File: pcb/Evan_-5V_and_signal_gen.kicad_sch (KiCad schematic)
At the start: 24 parts, among them IC1 TL7660IDGKR, IC2 TL081IDT, IC4 UA78M33CDCYG3, J2 M22-6003005

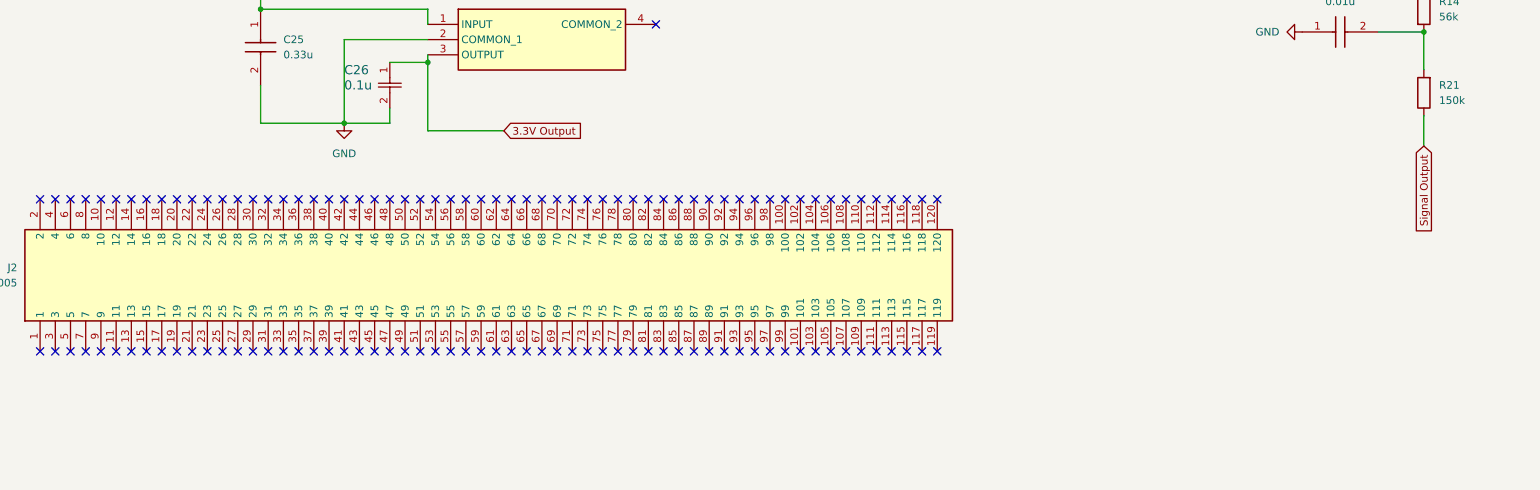
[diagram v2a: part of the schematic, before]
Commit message: First Major PCB layout and routing (#10)
* first bulk commit of routing

* removed about 300 pcb ERC warnings

* removed all pcb DRC errors/warnings

* silkscreen: remove part num from inside part, cleanup

* add silk labels for each pin, my final cleanup

* remove all errors and suppress unspecified connections warnings in schematic ERC

---------

Co-authored-by: evanc2987 <evan.campbell2987@gmail.com>
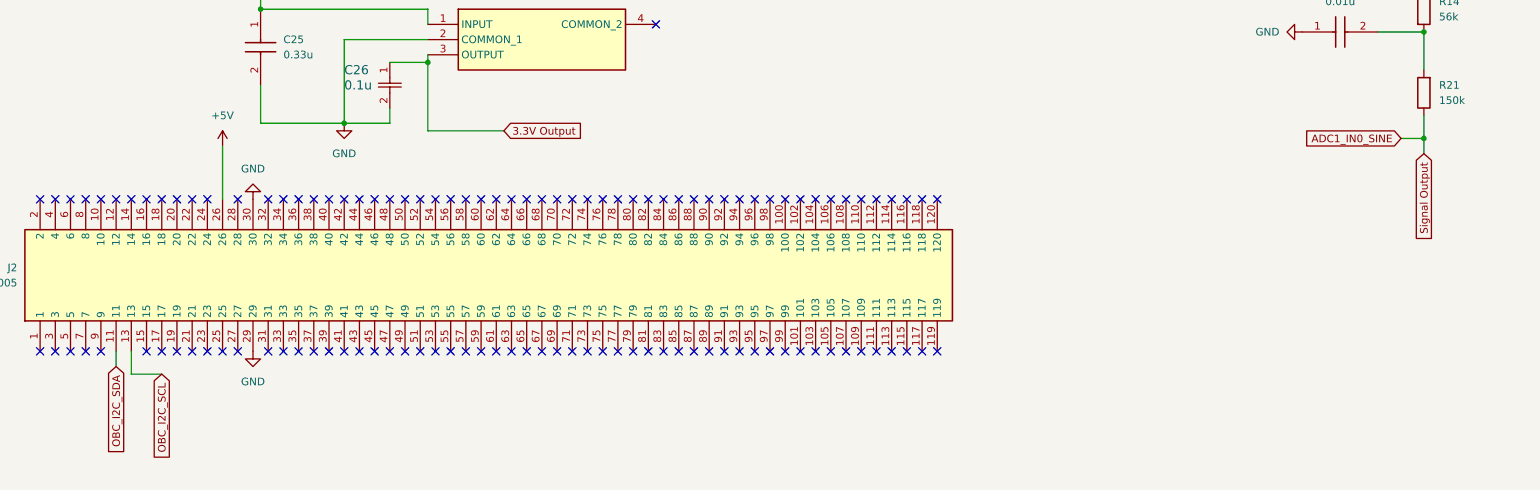
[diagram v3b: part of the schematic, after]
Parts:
- C12, C13: footprint T495D -> (none)
- C17, C18, C25: footprint C0805 -> (none)
- IC1: footprint SOP65P490X110-8N -> capstone:SOIC127P600X175-8N
- IC2: footprint SOIC127P600X175-8N -> capstone:SOIC127P600X175-8N
- IC4: footprint SOT230P700X180-4N -> (none)
- J2: footprint RHDR120W55P200_4X30_6020X800X935P -> capstone:RHDR120W55P200_4X30_6020X800X935P
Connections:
- net +5V: now also J2.26
- net GND: now also J2.29, J2.30
- net OBC_I2C_SDA: now reaches J2.11
- net OBC_I2C_SCL: now reaches J2.13
- net Signal Output renamed ADC1_IN0_SINE
- no-connect marks 124 -> 119
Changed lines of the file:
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@@
   (junction (at 82.55 38.1) (diameter 0) (color 0 0 0 0)
+  )
+  (junction (at 262.89 123.19) (diameter 0) (color 0 0 0 0)
   )
   (junction (at 156.21 22.86) (diameter 0) (color 0 0 0 0)
@@
   (no_connect (at 85.09 133.35))
   (no_connect (at 97.79 133.35))
-  (no_connect (at 69.85 133.35))
   (no_connect (at 92.71 133.35))
   (no_connect (at 39.37 158.75))
@@
   (no_connect (at 146.05 133.35))
   (no_connect (at 46.99 133.35))
-  (no_connect (at 44.45 158.75))
   (no_connect (at 176.53 133.35))
   (no_connect (at 176.53 158.75))
@@
   (no_connect (at 163.83 133.35))
   (no_connect (at 49.53 158.75))
-  (no_connect (at 67.31 133.35))
   (no_connect (at 123.19 133.35))
   (no_connect (at 77.47 133.35))
@@
   (no_connect (at 41.91 158.75))
   (no_connect (at 80.01 158.75))
+  (no_connect (at 69.85 133.35))
   (no_connect (at 166.37 133.35))
   (no_connect (at 171.45 133.35))
   (no_connect (at 74.93 158.75))
   (no_connect (at 64.77 133.35))
+  (no_connect (at 82.55 158.75))
   (no_connect (at 138.43 133.35))
   (no_connect (at 181.61 133.35))
@@
   (no_connect (at 80.01 133.35))
   (no_connect (at 138.43 158.75))
-  (no_connect (at 46.99 158.75))
   (no_connect (at 123.19 158.75))
   (no_connect (at 171.45 158.75))
@@
   (no_connect (at 77.47 158.75))
   (no_connect (at 100.33 158.75))
-  (no_connect (at 67.31 158.75))
   (no_connect (at 69.85 158.75))
   (no_connect (at 148.59 133.35))
@@
   (no_connect (at 52.07 133.35))
   (no_connect (at 59.69 158.75))
-  (no_connect (at 82.55 158.75))
   (no_connect (at 34.29 158.75))
   (no_connect (at 59.69 133.35))
-  (no_connect (at 62.23 133.35))
   (no_connect (at 41.91 133.35))
   (no_connect (at 49.53 133.35))
   (no_connect (at 102.87 158.75))
   (no_connect (at 54.61 133.35))
+  (no_connect (at 85.09 158.75))
   (no_connect (at 115.57 133.35))
   (no_connect (at 110.49 133.35))
@@
   (no_connect (at 95.25 158.75))
   (no_connect (at 97.79 158.75))
-  (no_connect (at 85.09 158.75))
   (no_connect (at 153.67 133.35))
   (no_connect (at 90.17 158.75))
@@
     (stroke (width 0) (type default))
   )
+  (wire (pts (xy 44.45 158.75) (xy 44.45 161.29))
+    (stroke (width 0) (type default))
+  )
   (wire (pts (xy 95.25 35.56) (xy 73.66 35.56))
     (stroke (width 0) (type default))
@@
     (stroke (width 0) (type default))
   )
+  (wire (pts (xy 262.89 123.19) (xy 262.89 125.73))
+    (stroke (width 0) (type default))
+  )
   (wire (pts (xy 104.14 38.1) (xy 113.03 38.1))
     (stroke (width 0) (type default))
@@
     (stroke (width 0) (type default))
   )
+  (wire (pts (xy 46.99 162.56) (xy 46.99 158.75))
+    (stroke (width 0) (type default))
+  )
   (wire (pts (xy 217.17 71.12) (xy 262.89 71.12))
     (stroke (width 0) (type default))
@@
     (stroke (width 0) (type default))
   )
+  (wire (pts (xy 259.08 123.19) (xy 262.89 123.19))
+    (stroke (width 0) (type default))
+  )
   (wire (pts (xy 158.75 71.12) (xy 147.32 71.12))
     (stroke (width 0) (type default))
@@
     (stroke (width 0) (type default))
   )
+  (wire (pts (xy 52.07 162.56) (xy 46.99 162.56))
+    (stroke (width 0) (type default))
+  )
   (wire (pts (xy 82.55 38.1) (xy 104.14 38.1))
     (stroke (width 0) (type default))
@@
     (stroke (width 0) (type default))
   )
-  (wire (pts (xy 262.89 119.38) (xy 262.89 124.46))
-    (stroke (width 0) (type default))
-  )
-  (global_label "Signal Output" (shape input) (at 262.89 124.46 270) (fields_autoplaced)
+  (wire (pts (xy 62.23 124.46) (xy 62.23 133.35))
+    (stroke (width 0) (type default))
+  )
+  (wire (pts (xy 262.89 119.38) (xy 262.89 123.19))
+    (stroke (width 0) (type default))
+  )
+  (global_label "ADC1_IN0_SINE" (shape input) (at 259.08 123.19 180) (fields_autoplaced)
     (effects (font (size 1.27 1.27)) (justify right))
-    (property "Intersheetrefs" "${INTERSHEET_REFS}" (at 262.89 140.5682 90)
+    (property "Intersheetrefs" "${INTERSHEET_REFS}" (at 241.8829 123.19 0)
+      (effects (font (size 1.27 1.27)) (justify right) hide)
+    )
+  )
+  (global_label "Signal Output" (shape input) (at 262.89 125.73 270) (fields_autoplaced)
+    (effects (font (size 1.27 1.27)) (justify right))
+    (property "Intersheetrefs" "${INTERSHEET_REFS}" (at 262.89 141.8382 90)
       (effects (font (size 1.27 1.27)) (justify right) hide)
     )
@@
     )
   )
+  (global_label "OBC_I2C_SDA" (shape input) (at 44.45 161.29 270) (fields_autoplaced)
+    (effects (font (size 1.27 1.27)) (justify right))
+    (property "Intersheetrefs" "${INTERSHEET_REFS}" (at 44.45 176.7333 90)
+      (effects (font (size 1.27 1.27)) (justify right) hide)
+    )
+  )
+  (global_label "OBC_I2C_SCL" (shape input) (at 52.07 162.56 270) (fields_autoplaced)
+    (effects (font (size 1.27 1.27)) (justify right))
+    (property "Intersheetrefs" "${INTERSHEET_REFS}" (at 52.07 177.9428 90)
+      (effects (font (size 1.27 1.27)) (justify right) hide)
+    )
+  )
   (global_label "3.3V Output" (shape input) (at 109.22 121.92 0) (fields_autoplaced)
     (effects (font (size 1.27 1.27)) (justify left))
@@
       (effects (font (size 1.27 1.27)) (justify right))
     )
-    (property "Footprint" "T495D" (at 178.74 44.45 0)
+    (property "Footprint" "" (at 178.74 44.45 0)
       (effects (font (size 1.27 1.27)) (justify left top) hide)
     )
@@
       (effects (font (size 1.27 1.27)) (justify left))
     )
-    (property "Footprint" "RHDR120W55P200_4X30_6020X800X935P" (at 126.67 137.16 0)
+    (property "Footprint" "capstone:RHDR120W55P200_4X30_6020X800X935P" (at 126.67 137.16 0)
       (effects (font (size 1.27 1.27)) (justify left top) hide)
     )
@@
     )
   )
+  (symbol (lib_id "power:GND") (at 67.31 158.75 0) (unit 1)
+    (in_bom yes) (on_board yes) (dnp no) (fields_autoplaced)
+    (property "Reference" "#PWR014" (at 67.31 165.1 0)
+      (effects (font (size 1.27 1.27)) hide)
+    )
+    (property "Value" "GND" (at 67.31 163.83 0)
+      (effects (font (size 1.27 1.27)))
+    )
+    (property "Footprint" "" (at 67.31 158.75 0)
+      (effects (font (size 1.27 1.27)) hide)
+    )
+    (property "Datasheet" "" (at 67.31 158.75 0)
+      (effects (font (size 1.27 1.27)) hide)
+    )
+    (pin "1")
+    (instances
+      (project "mcu_integration"
+        (path "/c0210bc3-f67f-47d8-a34e-f002a728adb2/39708197-8fe0-4b5c-ba49-65ed06982da9"
+          (reference "#PWR014") (unit 1)
+        )
+      )
+    )
+  )
   (symbol (lib_id "capstone:TL7660IDGKR") (at 43.18 30.48 0) (unit 1)
     (in_bom yes) (on_board yes) (dnp no) (fields_autoplaced)
@@
       (effects (font (size 1.27 1.27)))
     )
-    (property "Footprint" "SOP65P490X110-8N" (at 69.85 125.4 0)
+    (property "Footprint" "capstone:SOIC127P600X175-8N" (at 69.85 125.4 0)
       (effects (font (size 1.27 1.27)) (justify left top) hide)
     )
@@
       (effects (font (size 1.27 1.27)))
     )
-    (property "Footprint" "SOIC127P600X175-8N" (at 213.36 160.96 0)
+    (property "Footprint" "capstone:SOIC127P600X175-8N" (at 213.36 160.96 0)
       (effects (font (size 1.27 1.27)) (justify left top) hide)
     )
@@
       (effects (font (size 1.27 1.27)) (justify right))
     )
-    (property "Footprint" "C0805" (at 243.51 26.67 0)
+    (property "Footprint" "" (at 243.51 26.67 0)
       (effects (font (size 1.27 1.27)) (justify left top) hide)
     )
@@
       (effects (font (size 1.27 1.27)) (justify left))
     )
-    (property "Footprint" "T495D" (at -80.95 38.1 0)
+    (property "Footprint" "" (at -80.95 38.1 0)
       (effects (font (size 1.27 1.27)) (justify left top) hide)
     )
@@
       (effects (font (size 1.27 1.27)))
     )
-    (property "Footprint" "C0805" (at 251.46 201.6 0)
+    (property "Footprint" "" (at 251.46 201.6 0)
       (effects (font (size 1.27 1.27)) (justify left top) hide)
     )
@@
       (effects (font (size 1.27 1.27)) (justify left))
     )
-    (property "Footprint" "C0805" (at -27.61 110.49 0)
+    (property "Footprint" "" (at -27.61 110.49 0)
       (effects (font (size 1.27 1.27)) (justify left top) hide)
     )
@@
     )
   )
+  (symbol (lib_id "power:GND") (at 67.31 133.35 180) (unit 1)
+    (in_bom yes) (on_board yes) (dnp no) (fields_autoplaced)
+    (property "Reference" "#PWR02" (at 67.31 127 0)
+      (effects (font (size 1.27 1.27)) hide)
+    )
+    (property "Value" "GND" (at 67.31 128.27 0)
+      (effects (font (size 1.27 1.27)))
+    )
+    (property "Footprint" "" (at 67.31 133.35 0)
+      (effects (font (size 1.27 1.27)) hide)
+    )
+    (property "Datasheet" "" (at 67.31 133.35 0)
+      (effects (font (size 1.27 1.27)) hide)
+    )
+    (pin "1")
+    (instances
+      (project "mcu_integration"
+        (path "/c0210bc3-f67f-47d8-a34e-f002a728adb2/39708197-8fe0-4b5c-ba49-65ed06982da9"
+          (reference "#PWR02") (unit 1)
+        )
+      )
+    )
+  )
   (symbol (lib_id "power:GND") (at 129.54 81.28 0) (unit 1)
     (in_bom yes) (on_board yes) (dnp no) (fields_autoplaced)
@@
       (effects (font (size 1.27 1.27)))
     )
-    (property "Footprint" "SOT230P700X180-4N" (at 130.81 199.06 0)
+    (property "Footprint" "" (at 130.81 199.06 0)
       (effects (font (size 1.27 1.27)) (justify left top) hide)
     )
@@
         )
       )
+    )
+  )
+  (symbol (lib_id "power:+5V") (at 62.23 124.46 0) (unit 1)
+    (in_bom yes) (on_board yes) (dnp no) (fields_autoplaced)
+    (property "Reference" "#PWR016" (at 62.23 128.27 0)
+      (effects (font (size 1.27 1.27)) hide)
+    )
+    (property "Value" "+5V" (at 62.23 119.38 0)
+      (effects (font (size 1.27 1.27)))
+    )
+    (property "Footprint" "" (at 62.23 124.46 0)
+      (effects (font (size 1.27 1.27)) hide)
+    )
+    (property "Datasheet" "" (at 62.23 124.46 0)
+      (effects (font (size 1.27 1.27)) hide)
+    )
+    (pin "1")
+    (instances
+      (project "mcu_integration"
+        (path "/c0210bc3-f67f-47d8-a34e-f002a728adb2/39708197-8fe0-4b5c-ba49-65ed06982da9"
+          (reference "#PWR016") (unit 1)
+        )
+      )

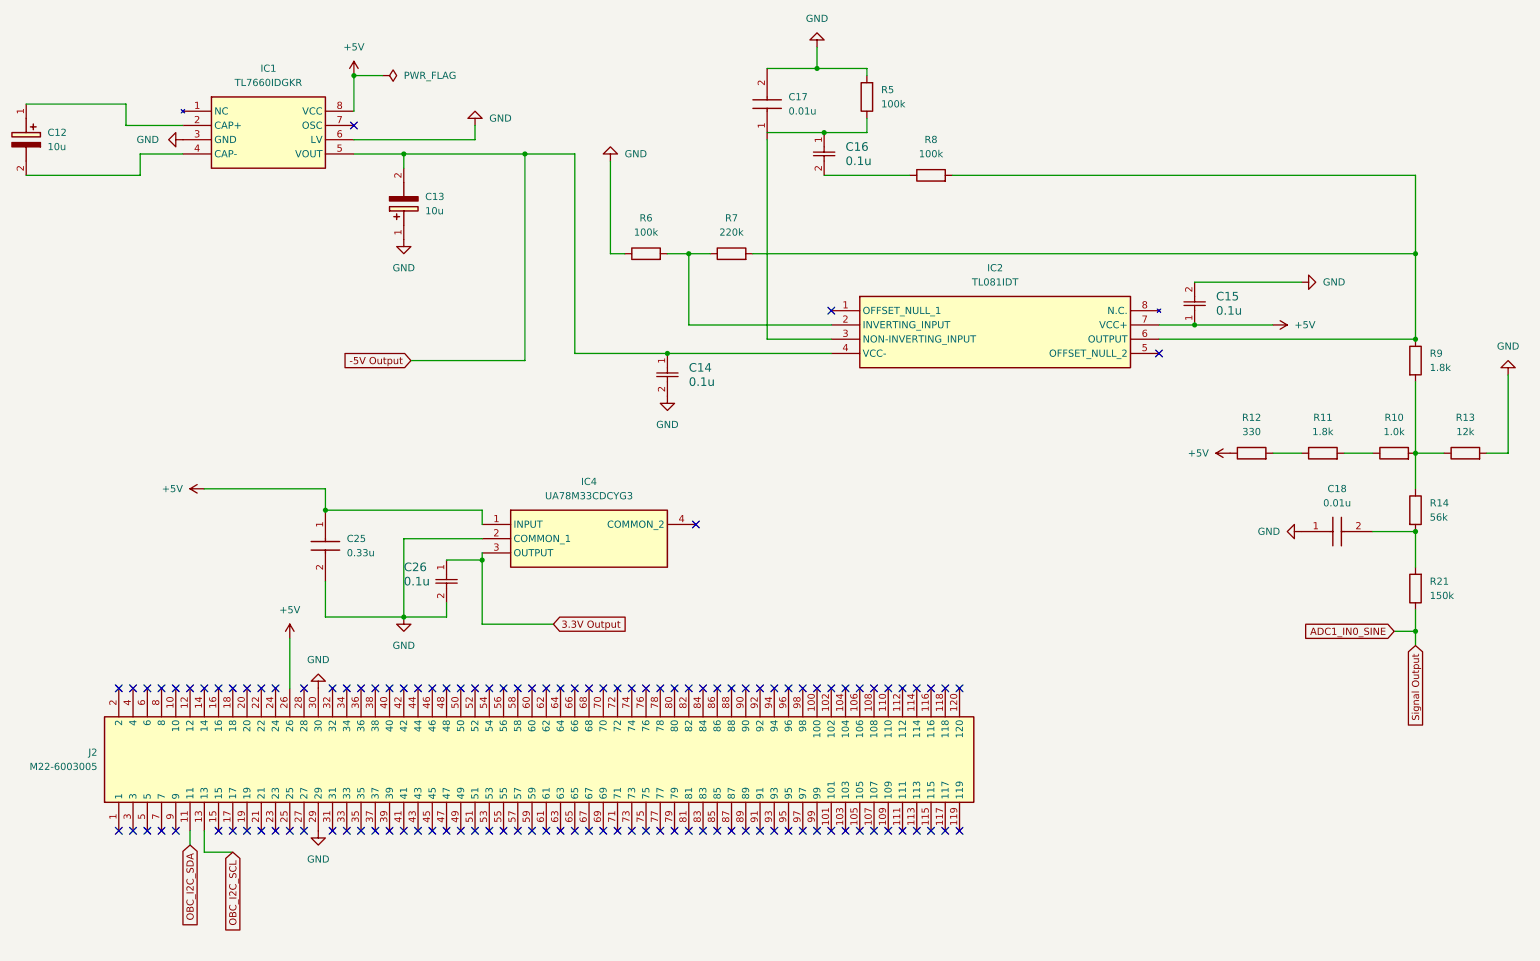
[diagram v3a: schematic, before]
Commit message: Wire touchup, initial changes (#12)
* Implemented mosfet, decoupling

Please review functionality

* wire placement, inital revisions

made it more PCB ready with spacing and such
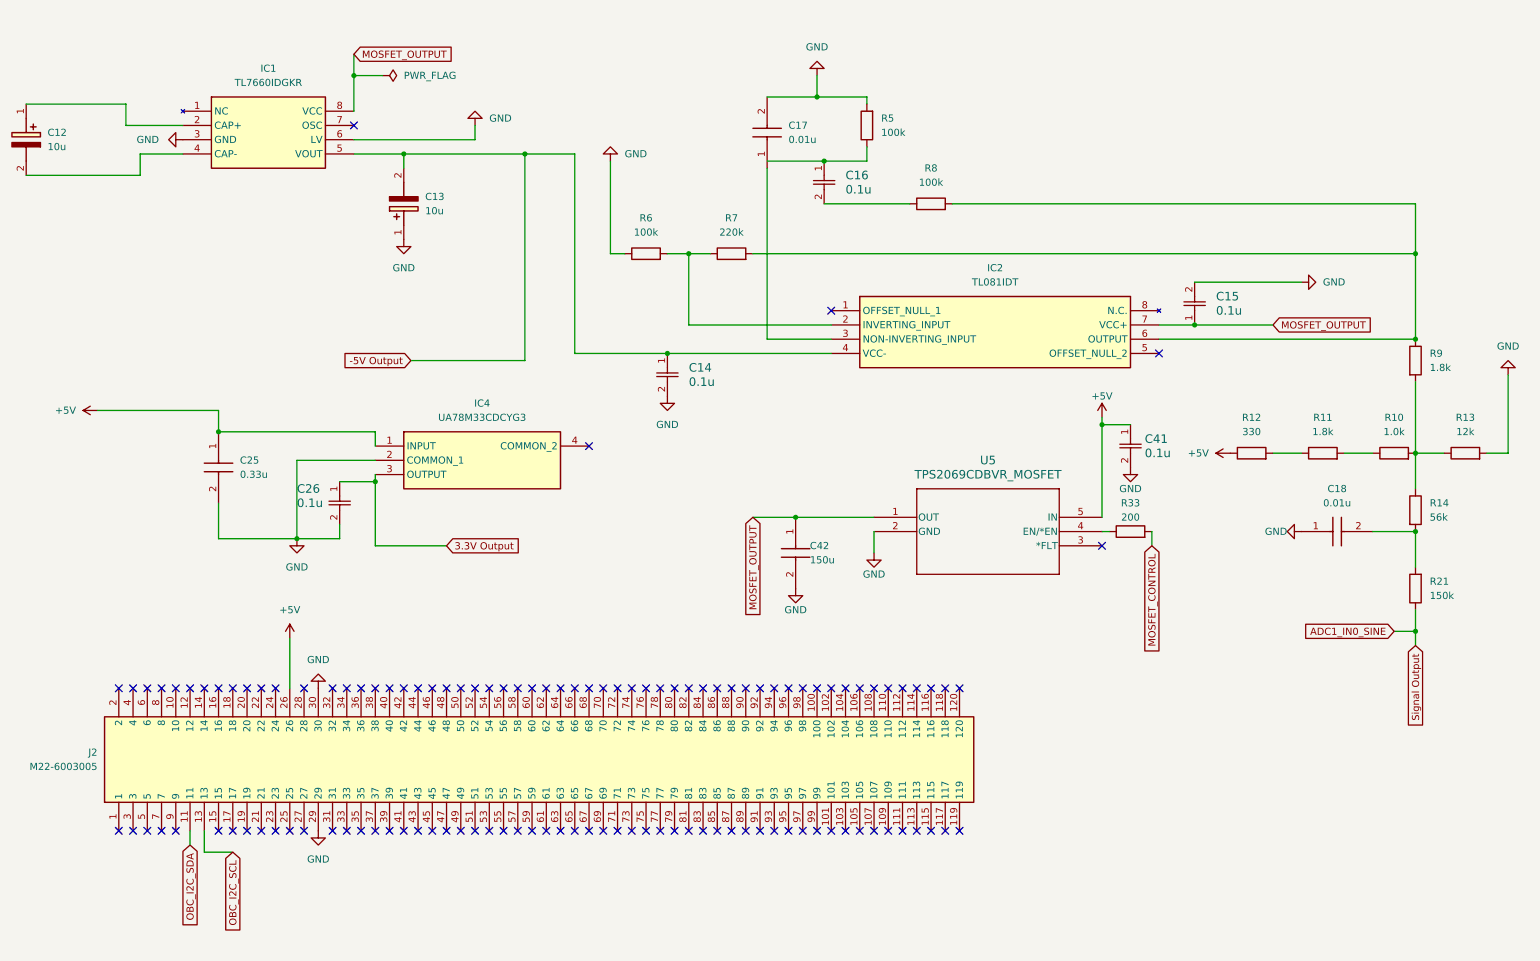
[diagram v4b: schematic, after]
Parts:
- added C41: 0.1u, capstone:CAPC220145_88N_KEM-0.1u, symbol capstone:C0805C104K5RAC7210
- added C42: 150u, capstone:CAPC3225X280N_150U, symbol capstone:CL32A157MQVNNNE_150u
- added R33: 200, Resistor_SMD:R_0402_1005Metric, symbol Device:R
- added U5: TPS2069CDBVR_MOSFET, capstone:DBV5_TEX_MF, symbol capstone:TPS2069CDBVR_MF
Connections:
- net +5V: now also C41.1, U5.5 (IN); no longer C15.1, IC1.8 (VCC), IC2.7 (VCC+)
- net GND: now also C41.2, C42.2, U5.2 (GND)
- new net: R33.1, U5.4 (EN/*EN)
- new net MOSFET_CONTROL: R33.2
- new net MOSFET_OUTPUT: C15.1, C42.1, IC1.8 (VCC), IC2.7 (VCC+), U5.1 (OUT)
- no-connect marks 119 -> 120
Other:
- moved on the sheet: C16, C17, C25, C26, IC4, R5, R8
